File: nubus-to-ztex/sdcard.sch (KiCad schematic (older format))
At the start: 3 parts, among them J2 47219-2001 (micro-sd)

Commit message: some BoM optimization
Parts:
- C2: MPN CC0603KRX7R8BB104 -> CC0603KRX7R9BB104; URL https://www.lcsc.com/product-detail/Multilayer-Ceramic-Capacitors-MLCC-SMD-SMT_YAGEO-CC0603KRX7R8BB104_C92490.html -> https://www.lcsc.com/product-detail/Multilayer-Ceramic-Capacitors-MLCC-SMD-SMT_YAGEO-CC0603KRX7R9BB104_C14663.html
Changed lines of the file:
@@
 F 3 "" H 5200 5150 50  0000 C CNN
 F 4 "www.yageo.com" H 5200 5150 50  0001 C CNN "MNF1_URL"
-F 5 "CC0603KRX7R8BB104" H 5200 5150 50  0001 C CNN "MPN"
+F 5 "CC0603KRX7R9BB104" H 5200 5150 50  0001 C CNN "MPN"
 F 6 "603-CC603KRX7R8BB104" H 5200 5150 50  0001 C CNN "Mouser"
 F 7 "?" H 5200 5150 50  0001 C CNN "Digikey"
@@
 F 9 "?" H 5200 5150 50  0001 C CNN "Koncar"
 F 10 "TB" H 5200 5150 50  0001 C CNN "Side"
-F 11 "https://www.lcsc.com/product-detail/Multilayer-Ceramic-Capacitors-MLCC-SMD-SMT_YAGEO-CC0603KRX7R8BB104_C92490.html" H 3000 6050 50  0001 C CNN "URL"
+F 11 "https://www.lcsc.com/product-detail/Multilayer-Ceramic-Capacitors-MLCC-SMD-SMT_YAGEO-CC0603KRX7R9BB104_C14663.html" H 3000 6050 50  0001 C CNN "URL"
 	1    5200 5150
 	1    0    0    -1

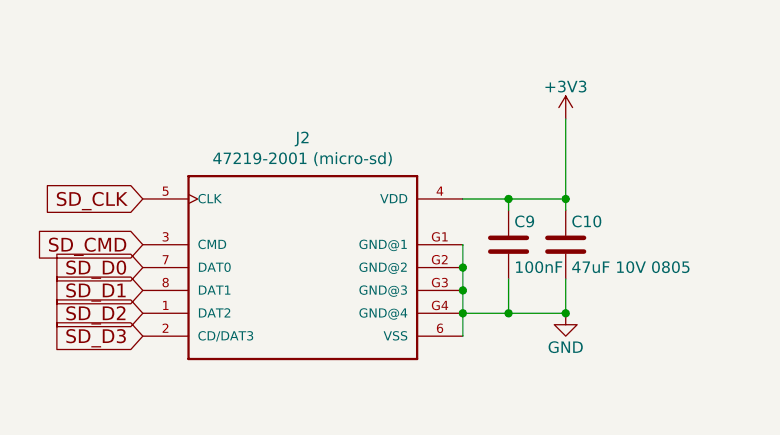
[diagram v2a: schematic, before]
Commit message: more JLCPCB BoM optimization
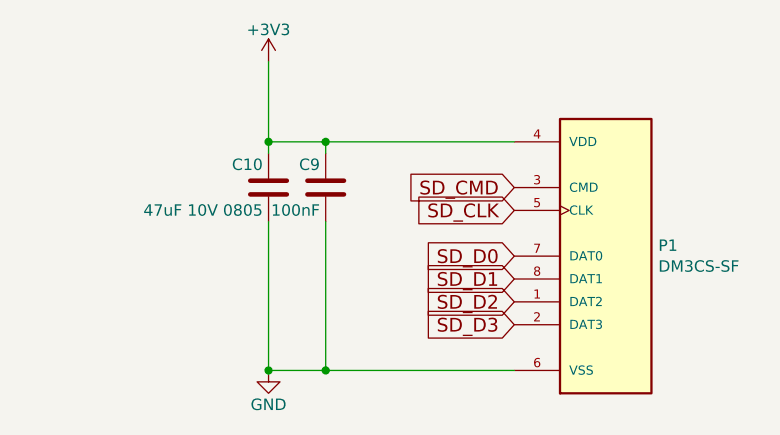
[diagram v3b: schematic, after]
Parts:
- removed J2: 47219-2001 (micro-sd), MOLEX_47219-2001:MOLEX_47219-2001, symbol 47219-2001:47219-2001
- added P1: DM3CS-SF, For_SeeedStudio:HRS_DM3CS-SF, symbol DM3CS-SF:DM3CS-SF
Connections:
- net +3V3: now also P1.4 (VDD)
- net GND: now also P1.6 (VSS)
- net SD_CLK: now also P1.5 (CLK)
- net SD_CMD: now also P1.3 (CMD)
- net SD_D0: now also P1.7 (DAT0)
- net SD_D1: now also P1.8 (DAT1)
- net SD_D2: now also P1.1 (DAT2)
- net SD_D3: now also P1.2 (DAT3)
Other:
- moved on the sheet: C10, C9
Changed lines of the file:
@@
 L power:GND #PWR0124
 U 1 1 58DA7C71
-P 5450 5450
-F 0 "#PWR0124" H 5450 5200 50  0001 C CNN
-F 1 "GND" H 5450 5300 50  0000 C CNN
-F 2 "" H 5450 5450 50  0000 C CNN
-F 3 "" H 5450 5450 50  0000 C CNN
-	1    5450 5450
-	1    0    0    -1
+P 4150 5700
+F 0 "#PWR0124" H 4150 5450 50  0001 C CNN
+F 1 "GND" H 4150 5550 50  0000 C CNN
+F 2 "" H 4150 5700 50  0000 C CNN
+F 3 "" H 4150 5700 50  0000 C CNN
+	1    4150 5700
+	-1   0    0    -1
 $EndComp
 $Comp
 L power:+3V3 #PWR0125
 U 1 1 58DA7C72
-P 5450 4600
-F 0 "#PWR0125" H 5450 4450 50  0001 C CNN
-F 1 "+3V3" H 5450 4740 50  0000 C CNN
-F 2 "" H 5450 4600 50  0000 C CNN
-F 3 "" H 5450 4600 50  0000 C CNN
-	1    5450 4600
-	1    0    0    -1
+P 4150 4350
+F 0 "#PWR0125" H 4150 4200 50  0001 C CNN
+F 1 "+3V3" H 4150 4490 50  0000 C CNN
+F 2 "" H 4150 4350 50  0000 C CNN
+F 3 "" H 4150 4350 50  0000 C CNN
+	1    4150 4350
+	-1   0    0    -1
 $EndComp
-Text GLabel 3600 5450 0    60   Input ~ 0
+Text GLabel 5225 5400 0    60   Input ~ 0
 SD_D2
-Text GLabel 3600 5550 0    60   Input ~ 0
+Text GLabel 5225 5500 0    60   Input ~ 0
 SD_D3
-Text GLabel 3600 5150 0    60   Input ~ 0
+Text GLabel 5225 4900 0    60   Input ~ 0
 SD_CMD
-Text GLabel 3600 4950 0    60   Input ~ 0
+Text GLabel 5225 5000 0    60   Input ~ 0
 SD_CLK
-Text GLabel 3600 5250 0    60   Input ~ 0
+Text GLabel 5225 5200 0    60   Input ~ 0
 SD_D0
-Text GLabel 3600 5350 0    60   Input ~ 0
+Text GLabel 5225 5300 0    60   Input ~ 0
 SD_D1
 $Comp
 L Device:C C10
 U 1 1 590C7447
-P 5450 5150
-F 0 "C10" H 5475 5250 50  0000 L CNN
-F 1 "47uF 10V 0805" H 5475 5050 50  0000 L CNN
-F 2 "Capacitor_SMD:C_0805_2012Metric" H 5488 5000 50  0001 C CNN
-F 3 "" H 5450 5150 50  0000 C CNN
-F 4 "GRM21BR60J476ME15L" H 5450 5150 50  0001 C CNN "MPN-ALT"
-F 5 "https://www.lcsc.com/product-detail/Multilayer-Ceramic-Capacitors-MLCC-SMD-SMT_Murata-Electronics-GRM21BR60J476ME15L_C77072.html" H 5450 5150 50  0001 C CNN "URL-ALT"
-F 6 "C2012X5R1A476MTJ00E" H 5450 5150 50  0001 C CNN "MPN"
-F 7 "https://www.lcsc.com/product-detail/Multilayer-Ceramic-Capacitors-MLCC-SMD-SMT_TDK-C2012X5R1A476MTJ00E_C76636.html" H 5450 5150 50  0001 C CNN "URL"
-	1    5450 5150
-	1    0    0    -1
-$EndComp
-$Comp
-L 47219-2001:47219-2001 J2
-U 1 1 5F6F557B
-P 4300 5250
-F 0 "J2" H 4300 5817 50  0000 C CNN
-F 1 "47219-2001 (micro-sd)" H 4300 5726 50  0000 C CNN
-F 2 "MOLEX_47219-2001:MOLEX_47219-2001" H 4300 5250 50  0001 L BNN
-F 3 "https://www.molex.com/webdocs/datasheets/pdf/en-us/0472192001_MEMORY_CARD_SOCKET.pdf" H 4300 5250 50  0001 L BNN
-F 4 "47219-2001" H 4300 5250 50  0001 C CNN "MPN"
-F 5 "https://www.lcsc.com/product-detail/SD-Card-Connectors_MOLEX-472192001_C164170.html" H 4300 5250 50  0001 C CNN "URL"
-	1    4300 5250
-	1    0    0    -1
+P 4150 4900
+F 0 "C10" H 4175 5000 50  0000 L CNN
+F 1 "47uF 10V 0805" H 4175 4800 50  0000 L CNN
+F 2 "Capacitor_SMD:C_0805_2012Metric" H 4188 4750 50  0001 C CNN
+F 3 "" H 4150 4900 50  0000 C CNN
+F 4 "GRM21BR60J476ME15L" H 4150 4900 50  0001 C CNN "MPN-ALT"
+F 5 "https://www.lcsc.com/product-detail/Multilayer-Ceramic-Capacitors-MLCC-SMD-SMT_Murata-Electronics-GRM21BR60J476ME15L_C77072.html" H 4150 4900 50  0001 C CNN "URL-ALT"
+F 6 "C2012X5R1A476MTJ00E" H 4150 4900 50  0001 C CNN "MPN"
+F 7 "https://www.lcsc.com/product-detail/Multilayer-Ceramic-Capacitors-MLCC-SMD-SMT_TDK-C2012X5R1A476MTJ00E_C76636.html" H 4150 4900 50  0001 C CNN "URL"
+	1    4150 4900
+	-1   0    0    -1
 $EndComp
 Wire Wire Line
-	5450 5450 5200 5450
+	4150 5700 4400 5700
+Connection ~ 4150 5700
+Connection ~ 4150 4700
 Wire Wire Line
-	5000 5450 5000 5350
-Connection ~ 5000 5450
-Wire Wire Line
-	5000 5350 5000 5250
-Connection ~ 5000 5350
-Wire Wire Line
-	5000 5250 5000 5150
-Connection ~ 5000 5250
-Wire Wire Line
-	5000 5550 5000 5450
-Wire Wire Line
-	5450 5300 5450 5450
-Connection ~ 5450 5450
-Wire Wire Line
-	5000 4950 5200 4950
-Connection ~ 5450 4950
-Wire Wire Line
-	5450 4950 5450 5000
+	4150 4700 4150 4750
 $Comp
 L Device:C C?
 U 1 1 60D77AD6
-P 5200 5150
+P 4400 4900
 AR Path="/5F679B53/60D77AD6" Ref="C?"  Part="1"
 AR Path="/5F69F4EF/60D77AD6" Ref="C2"  Part="1"
 AR Path="/619D66B7/60D77AD6" Ref="C15"  Part="1"
 AR Path="/62D70B59/60D77AD6" Ref="C9"  Part="1"
-F 0 "C9" H 5225 5250 50  0000 L CNN
-F 1 "100nF" H 5225 5050 50  0000 L CNN
-F 2 "Capacitor_SMD:C_0603_1608Metric" H 5238 5000 50  0001 C CNN
-F 3 "" H 5200 5150 50  0000 C CNN
-F 4 "www.yageo.com" H 5200 5150 50  0001 C CNN "MNF1_URL"
-F 5 "CC0603KRX7R9BB104" H 5200 5150 50  0001 C CNN "MPN"
-F 6 "603-CC603KRX7R8BB104" H 5200 5150 50  0001 C CNN "Mouser"
-F 7 "?" H 5200 5150 50  0001 C CNN "Digikey"
-F 8 "" H 5200 5150 50  0001 C CNN "LCSC"
-F 9 "?" H 5200 5150 50  0001 C CNN "Koncar"
-F 10 "TB" H 5200 5150 50  0001 C CNN "Side"
-F 11 "https://www.lcsc.com/product-detail/Multilayer-Ceramic-Capacitors-MLCC-SMD-SMT_YAGEO-CC0603KRX7R9BB104_C14663.html" H 3000 6050 50  0001 C CNN "URL"
-	1    5200 5150
+F 0 "C9" H 4425 5000 50  0000 L CNN
+F 1 "100nF" H 4425 4800 50  0000 L CNN
+F 2 "Capacitor_SMD:C_0603_1608Metric" H 4438 4750 50  0001 C CNN
+F 3 "" H 4400 4900 50  0000 C CNN
+F 4 "www.yageo.com" H 4400 4900 50  0001 C CNN "MNF1_URL"
+F 5 "CC0603KRX7R9BB104" H 4400 4900 50  0001 C CNN "MPN"
+F 6 "603-CC603KRX7R8BB104" H 4400 4900 50  0001 C CNN "Mouser"
+F 7 "?" H 4400 4900 50  0001 C CNN "Digikey"
+F 8 "" H 4400 4900 50  0001 C CNN "LCSC"
+F 9 "?" H 4400 4900 50  0001 C CNN "Koncar"
+F 10 "TB" H 4400 4900 50  0001 C CNN "Side"
+F 11 "https://www.lcsc.com/product-detail/Multilayer-Ceramic-Capacitors-MLCC-SMD-SMT_YAGEO-CC0603KRX7R9BB104_C14663.html" H 2200 5800 50  0001 C CNN "URL"
+	1    4400 4900
+	-1   0    0    -1
+$EndComp
+Wire Wire Line
+	4400 4750 4400 4700
+Connection ~ 4400 4700
+Wire Wire Line
+	4400 4700 4150 4700
+Connection ~ 4400 5700
+Wire Wire Line
+	4150 4350 4150 4700
+$Comp
+L DM3CS-SF:DM3CS-SF P1
+U 1 1 641CE916
+P 5525 5200
+F 0 "P1" H 5855 5246 50  0000 L CNN
+F 1 "DM3CS-SF" H 5855 5155 50  0000 L CNN
+F 2 "For_SeeedStudio:HRS_DM3CS-SF" H 5525 5200 50  0001 L BNN
+F 3 "" H 5525 5200 50  0001 L BNN
+F 4 "Hirose Electric Co Ltd" H 5525 5200 50  0001 L BNN "MANUFACTURER"
+F 5 "DM3CS-SF" H 5525 5200 50  0001 C CNN "MPN"
+F 6 "https://www.lcsc.com/product-detail/SD-Card-Connectors_HRS-Hirose-DM3CS-SF_C202111.html" H 5525 5200 50  0001 C CNN "URL"
+	1    5525 5200
 	1    0    0    -1
 $EndComp
 Wire Wire Line
-	5200 5000 5200 4950
-Connection ~ 5200 4950
+	4150 5050 4150 5700
 Wire Wire Line
-	5200 4950 5450 4950
+	4400 5050 4400 5700
 Wire Wire Line
-	5200 5300 5200 5450
-Connection ~ 5200 5450
+	4400 5700 5225 5700
 Wire Wire Line
-	5200 5450 5000 5450
-Wire Wire Line
-	5450 4600 5450 4950
+	4400 4700 5225 4700
 $EndSCHEMATC

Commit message: even more JLCPCB BoM optimization
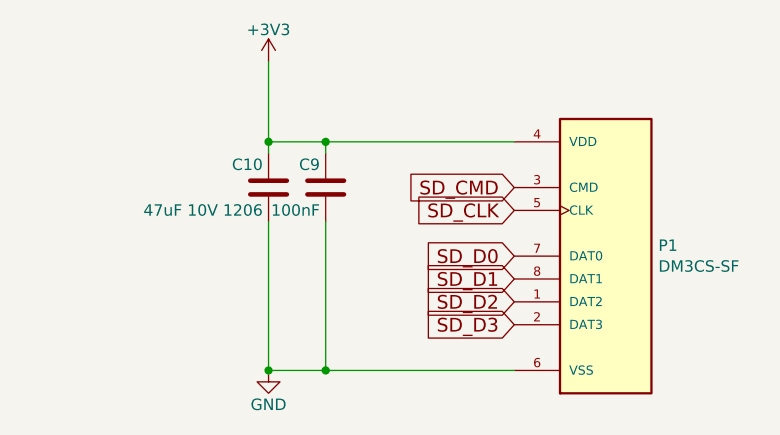
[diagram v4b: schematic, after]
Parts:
- C10: value 47uF 10V 0805 -> 47uF 10V 1206; footprint Capacitor_SMD:C_0805_2012Metric -> Capacitor_SMD:C_1206_3216Metric; MPN C2012X5R1A476MTJ00E -> CL31A476MPHNNNE; URL https://www.lcsc.com/product-detail/Multilayer-Ceramic-Capacitors-MLCC-SMD-SMT_TDK-C2012X5R1A476MTJ00E_C76636.html -> https://www.lcsc.com/product-detail/Multilayer-Ceramic-Capacitors-MLCC-SMD-SMT_Samsung-Electro-Mechanics-CL31A476MPHNNNE_C96123.html
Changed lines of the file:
@@
 P 4150 4900
 F 0 "C10" H 4175 5000 50  0000 L CNN
-F 1 "47uF 10V 0805" H 4175 4800 50  0000 L CNN
-F 2 "Capacitor_SMD:C_0805_2012Metric" H 4188 4750 50  0001 C CNN
+F 1 "47uF 10V 1206" H 4175 4800 50  0000 L CNN
+F 2 "Capacitor_SMD:C_1206_3216Metric" H 4188 4750 50  0001 C CNN
 F 3 "" H 4150 4900 50  0000 C CNN
 F 4 "GRM21BR60J476ME15L" H 4150 4900 50  0001 C CNN "MPN-ALT"
 F 5 "https://www.lcsc.com/product-detail/Multilayer-Ceramic-Capacitors-MLCC-SMD-SMT_Murata-Electronics-GRM21BR60J476ME15L_C77072.html" H 4150 4900 50  0001 C CNN "URL-ALT"
-F 6 "C2012X5R1A476MTJ00E" H 4150 4900 50  0001 C CNN "MPN"
-F 7 "https://www.lcsc.com/product-detail/Multilayer-Ceramic-Capacitors-MLCC-SMD-SMT_TDK-C2012X5R1A476MTJ00E_C76636.html" H 4150 4900 50  0001 C CNN "URL"
+F 6 "CL31A476MPHNNNE" H 4150 4900 50  0001 C CNN "MPN"
+F 7 "https://www.lcsc.com/product-detail/Multilayer-Ceramic-Capacitors-MLCC-SMD-SMT_Samsung-Electro-Mechanics-CL31A476MPHNNNE_C96123.html" H 4150 4900 50  0001 C CNN "URL"
 	1    4150 4900
 	-1   0    0    -1
